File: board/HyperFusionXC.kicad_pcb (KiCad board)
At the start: 2 copper layers, 102 x 65.5 mm, 142 parts, among them J1 Conn_01x03, J2 10067847-001RLF, J3 UJ20-C-H-G-SMT-2-P16-TR, J4 UJ20-C-H-G-SMT-2-P16-TR, J5 Conn_01x08, J6 Conn_01x05, J7 Conn_02x05_Odd_Even, Q1 UM6K34NTCN, U1 CONN_DF40C-120DP-0p4V51_120P_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, U10 SN74LVC1G04DCKR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

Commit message: Routing done
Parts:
- added C55: 100nF, Capacitor_SMD:C_0603_1608Metric, B.Cu at (123.9, 119.6)
- added C56: 4.7uF, Capacitor_SMD:C_0603_1608Metric, B.Cu at (123.9, 121.5)
- C105: value 4.7uF -> 100nF
- U1: value CONN_DF40C-120DP-0p4V51_120P_HIR -> SOM_FPGA_LP
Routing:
- net GNDA: track 129.3 -> 152.6 mm
- net GND: track 776.0 -> 784.9 mm, vias 22 -> 21
- net +5V: track 232.8 -> 237.8 mm
- net /TCK: track 48.6 -> 46.4 mm
- net /SD_WP: track 39.4 -> 41.2 mm
- net Net-(C18-Pad2): track 151.0 -> 152.5 mm
- net /ESP_BOOT_MODE: track 95.5 -> 96.5 mm
- net /HDDLED: track 57.6 -> 58.2 mm
- net /PUSH_BUTTON: track 66.7 -> 66.1 mm
- added copper zone on B.Cu, net GND
- added copper zone on F.Cu, net GND
- added copper zone on B.Cu, net GNDA
- added copper zone on F.Cu, net GNDA
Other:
- board text added: "HyperFusion XC V1.0 MSX Cartridge SHS 2026"
- board text added: "Line-Out"

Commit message: Improvements
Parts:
- added R41: 2k2, Resistor_SMD:R_0603_1608Metric, F.Cu at (101.9, 92.8)
- added R42: 2k2, Resistor_SMD:R_0603_1608Metric, F.Cu at (101.9, 94.4)
- added R51: 2k2, Resistor_SMD:R_0603_1608Metric, F.Cu at (176.5, 106.2)
- added R52: 2k2, Resistor_SMD:R_0603_1608Metric, F.Cu at (175.0, 106.2)
- C15, C18, C22: value 4.7uF -> 1uF
- C32: value 100nF -> 1uF
- U10: value SN74LVC1G04DCKR -> SN74LVC1G04DBVR
- moved C48 1.95 mm to (101.9, 96.1)
- moved C9 1.55 mm to (132.8, 90.0)
- moved C10 1.50 mm to (131.3, 90.0)
- moved R8 1.27 mm to (130.2, 97.7), turned to 90 degrees
- moved R9 1.25 mm to (129.5, 94.0), turned to 0 degrees
- moved C51 0.48 mm to (101.9, 98.0)
- moved C49 0.30 mm to (101.9, 91.2)
- moved C50 0.20 mm to (102.0, 99.6)
- turned C15 to 0 degrees
- turned R10 to 0 degrees
- turned R7 to 0 degrees
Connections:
- C15 pad 1: GND -> +3V3
- C15 pad 2: +3V3 -> GND
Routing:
- net Net-(U5-RMICP): track 2.46 -> 17.4 mm
- net +3V3: track 339.7 -> 350.6 mm, vias 17 -> 18
- net /LVDS_CLK_P: track 30.5 -> 25.7 mm
- net /LVDS_D2_N: track 29.6 -> 33.1 mm
- net Net-(U5-MICBIAS): track 3.20 -> 6.41 mm
- net Net-(X1-Pad44): track 14.6 -> 11.6 mm
- net Net-(U5-LMICP): track 5.84 -> 8.42 mm
- net /LVDS_D1_P: track 22.5 -> 24.5 mm
- net +IO1V8: track 84.3 -> 86.1 mm
- net Net-(J5-Pin_3): track 2.36 -> 4.01 mm
- net /LVDS_D0_N: track 27.5 -> 29.1 mm
- net /ESP_IO18/SDA: track 71.7 -> 73.3 mm, vias 4 -> 5
- net /LVDS_D1_N: track 26.0 -> 24.5 mm
- net /ESP_IO37/GP2: track 56.8 -> 55.3 mm
- net Net-(U5-LMICN): track 3.82 -> 2.51 mm
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
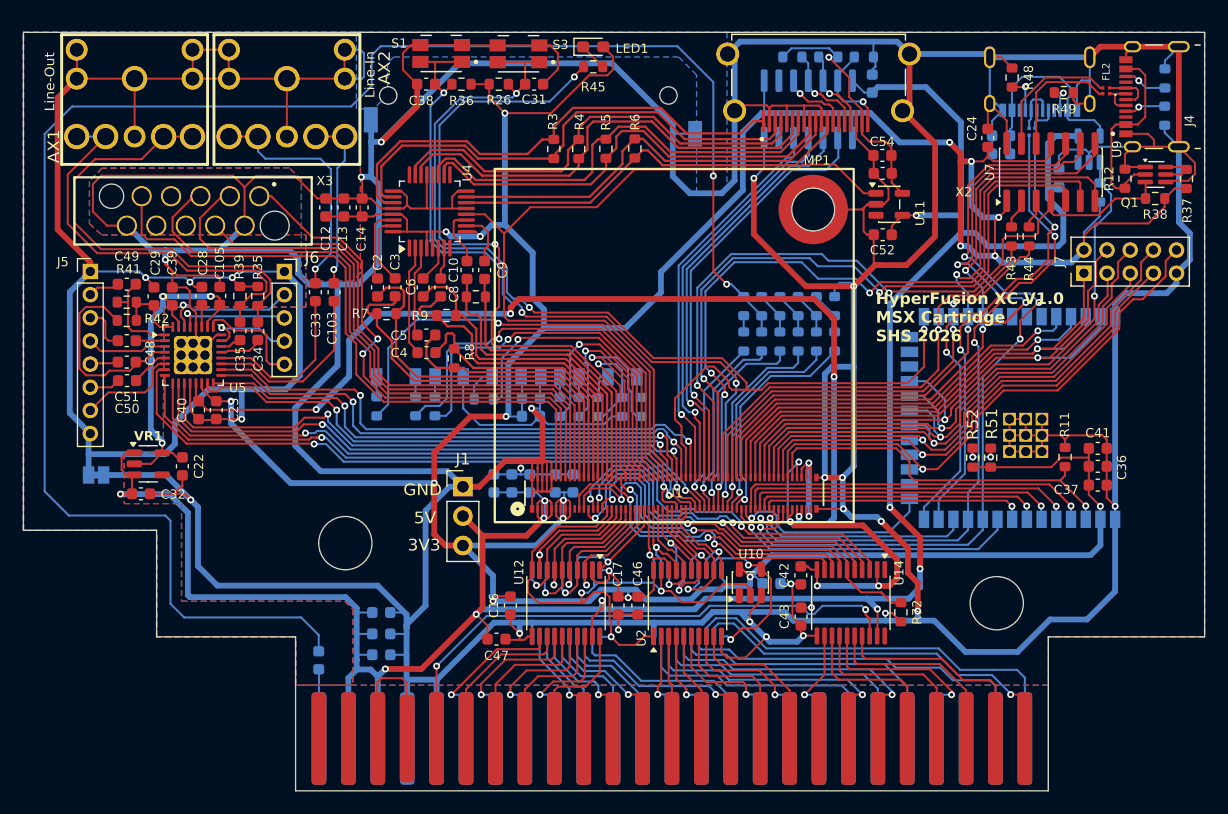
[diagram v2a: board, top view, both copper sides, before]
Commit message: Redesigned HDMI to solve obsolescence
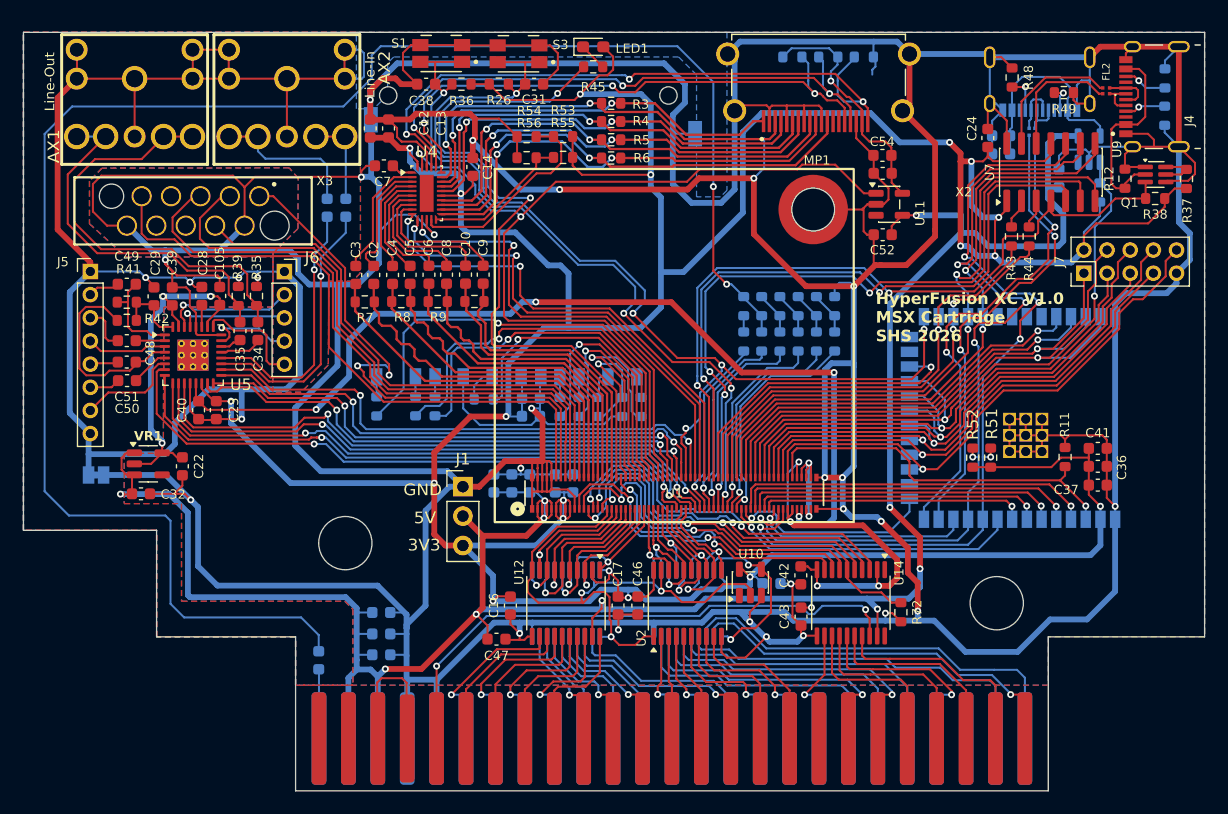
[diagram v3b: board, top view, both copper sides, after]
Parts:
- removed U15: TXB0104D, Package_SO:SOIC-14_3.9x8.7mm_P1.27mm
- added R53: 0E, Resistor_SMD:R_0603_1608Metric, F.Cu at (139.6, 78.5)
- added R54: 0E, Resistor_SMD:R_0603_1608Metric, F.Cu at (136.4, 78.5)
- added R55: 0E, Resistor_SMD:R_0603_1608Metric, F.Cu at (139.6, 80.3)
- added R56: 0E, Resistor_SMD:R_0603_1608Metric, F.Cu at (136.4, 80.3)
- C103, C33: moved to B.Cu
- C7: value 100nF -> 4.7uF; moved to F.Cu
- U4: value MAX3814 -> PI3HDX511DZLEX; footprint Package_QFP:TQFP-32_5x5mm_P0.5mm -> Package_DFN_QFN:Texas_RNH0030A_WQFN-30-1EP_2.5x4.5mm_P0.4mm_EP1.2x3.2mm
- U5: footprint Library:QFN-32-NAU88C22YG -> Library:QFN-32-1EP_5x5mm_P0.5mm_EP2.7x2.7mm_ThermalVias
- moved C7 42.8 mm to (124.1, 81.0), turned to 0 degrees
- moved C14 10.2 mm to (131.8, 81.1)
- moved C12 7.84 mm to (123.0, 77.8)
- moved C13 7.84 mm to (124.5, 77.8)
- moved C103 7.36 mm to (120.8, 84.7)
- moved C33 7.36 mm to (119.2, 84.7)
- moved C4 7.32 mm to (124.9, 90.5), turned to -90 degrees
- moved R8 6.70 mm to (125.6, 92.8), turned to 0 degrees
- moved R3 6.33 mm to (143.8, 75.6), turned to 180 degrees
- moved C5 5.38 mm to (126.4, 90.4), turned to -90 degrees
- moved R4 3.67 mm to (143.8, 77.2), turned to 180 degrees
- moved C3 3.56 mm to (121.7, 90.5)
- moved R6 2.21 mm to (143.8, 80.3), turned to 180 degrees
- moved R7 2.13 mm to (122.5, 92.8)
- moved U4 1.58 mm to (127.8, 83.4), turned to 0 degrees
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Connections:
- C10 pad 1: Net-(U4-IND-) -> Net-(U4-IN_CLK-)
- C2 pad 1: Net-(U4-INA+) -> Net-(U4-IN_D2+)
- C3 pad 1: Net-(U4-INA-) -> Net-(U4-IN_D2-)
- C4 pad 1: Net-(U4-INB+) -> Net-(U4-IN_D1-)
- C4 pad 2: /LVDS_D1_P -> /LVDS_D1_N
- C5 pad 1: Net-(U4-INB-) -> Net-(U4-IN_D1+)
- C5 pad 2: /LVDS_D1_N -> /LVDS_D1_P
- C6 pad 2: /LVDS_D0_P -> /LVDS_D0_N
- C7 pad 1: +5V -> GND
- C7 pad 2: GND -> Net-(U4-CEXT)
- C8 pad 2: /LVDS_D0_N -> /LVDS_D0_P
- C9 pad 1: Net-(U4-IND+) -> Net-(U4-IN_CLK+)
- R1 pad 2: Net-(U15-B2) -> /HDMI_C_SDA
- R2 pad 2: Net-(U15-B3) -> /HDMI_C_SCL
- R3 pad 1: /HDMI_A- -> /HDMI_A+
- R3 pad 2: /HDMI_A+ -> /HDMI_A-
- R4 pad 1: /HDMI_B- -> /HDMI_B+
- R4 pad 2: /HDMI_B+ -> /HDMI_B-
- R40 pad 1: Net-(U15-B1) -> /HDMI_C_HPD
- R5 pad 1: /HDMI_C- -> /HDMI_C+
- R5 pad 2: /HDMI_C+ -> /HDMI_C-
- R6 pad 1: /HDMI_D- -> /HDMI_D+
- R6 pad 2: /HDMI_D+ -> /HDMI_D-
- U1 pad 17: unconnected-(U1-B1-CLK1-Pad17) -> GND
- U1 pad 70: /HDMI_CEC -> /HDMI_SCL
- U1 pad 72: /HDMI_SCL -> /HDMI_SDA
- U1 pad 74: /HDMI_SDA -> /HDMI_HPD
- U1 pad 76: /HDMI_HPD -> /~{DBG_RST}
- U1 pad 78: /~{DBG_RST} -> /DBG_RXD
- U1 pad 80: /DBG_RXD -> /ESP_IO47
- U4 pad 1: unconnected-(U4-NC-Pad1) -> Net-(U4-CEXT)
- U4 pad 10: Net-(U4-IND+) -> /HDMI_HPD
- U4 pad 11: Net-(U4-IND-) -> /HDMI_SDA
- U4 pad 12: /~{HDMI_EN} -> /HDMI_SCL
- U4 pad 14: /HDMI_D- -> Net-(U4-OC_S0)
- U4 pad 15: /HDMI_D+ -> Net-(U4-EQ_S0)
- U4 pad 16: GND -> /HDMI_D+
- U4 pad 17: unconnected-(U4-NC-Pad17) -> /HDMI_D-
- U4 pad 18: /HDMI_C- -> /HDMI_C+
- U4 pad 19: /HDMI_C+ -> /HDMI_C-
- U4 pad 2: Net-(U4-INB+) -> Net-(U4-IN_D2-)
- U4 pad 20: GND -> +3V3
- U4 pad 21: GND -> /HDMI_B+
- U4 pad 23: /HDMI_B+ -> /HDMI_A+
- U4 pad 24: unconnected-(U4-NC-Pad24) -> /HDMI_A-
- U4 pad 25: GND -> /HDMI_C_SCL
- U4 pad 26: /HDMI_A- -> /HDMI_C_SDA
- U4 pad 27: /HDMI_A+ -> /HDMI_C_HPD
- U4 pad 29: +3V3 -> /~{HDMI_EN}
- U4 pad 3: Net-(U4-INB-) -> Net-(U4-IN_D2+)
- U4 pad 30: Net-(U4-INA+) -> +3V3
- U4 pad 31: Net-(U4-INA-) -> unconnected-(U4-NC-Pad31)
- U4 pad 4: +3V3 -> Net-(U4-IN_D1-)
- U4 pad 5: +3V3 -> Net-(U4-IN_D1+)
- U4 pad 8: unconnected-(U4-NC-Pad8) -> Net-(U4-IN_CLK-)
- U4 pad 9: +3V3 -> Net-(U4-IN_CLK+)
- U5 pad 33: GND -> unconnected-(U5-EXP-Pad33)_9
- U6 pad 24: unconnected-(U6-IO47-Pad24) -> /ESP_IO47
- X2 pad 13: Net-(U15-B4) -> unconnected-(X2-CEC-Pad13)
- X2 pad 15: Net-(U15-B3) -> /HDMI_C_SCL
- X2 pad 16: Net-(U15-B2) -> /HDMI_C_SDA
- X2 pad 19: Net-(U15-B1) -> /HDMI_C_HPD
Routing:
- net /HDMI_C_HPD: track 0.00 -> 56.5 mm, vias 0 -> 3
- net /HDMI_C_SDA: track 0.00 -> 51.0 mm, vias 0 -> 3
- net /HDMI_C_SCL: track 0.00 -> 49.8 mm, vias 0 -> 3
- net GND: track 783.6 -> 831.6 mm, vias 21 -> 24
- net /HDMI_CEC: track 34.4 -> 0.00 mm, vias 1 -> 0
- net /ESP_IO47: track 0.00 -> 26.7 mm, vias 0 -> 1
- net +5V: track 238.4 -> 219.1 mm
- net +3V3: track 350.6 -> 369.6 mm, vias 18 -> 19
- net Net-(U4-OC_S0): track 0.00 -> 18.1 mm
- net Net-(U4-EQ_S0): track 0.00 -> 12.9 mm
- net Net-(U4-IN_CLK+): track 0.00 -> 11.4 mm
- net Net-(U4-IN_CLK-): track 0.00 -> 11.4 mm
- net Net-(U4-IN_D2-): track 0.00 -> 10.6 mm
- net Net-(U4-IN_D2+): track 0.00 -> 10.4 mm
- net Net-(U4-INB+): track 9.55 -> 0.00 mm
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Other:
- board text removed: "R59"
